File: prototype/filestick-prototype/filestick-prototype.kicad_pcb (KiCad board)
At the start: 4 copper layers, 85 x 75 mm, 60 parts, among them J1 DIN-5, J2 DIN-5, J3 GPIO header 1, J4 UART header, J5 GPIO header 2, J6 SPI header, Q1 2N7002, Q2 2N7002, Q3 2N7002, Q4 2N7002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

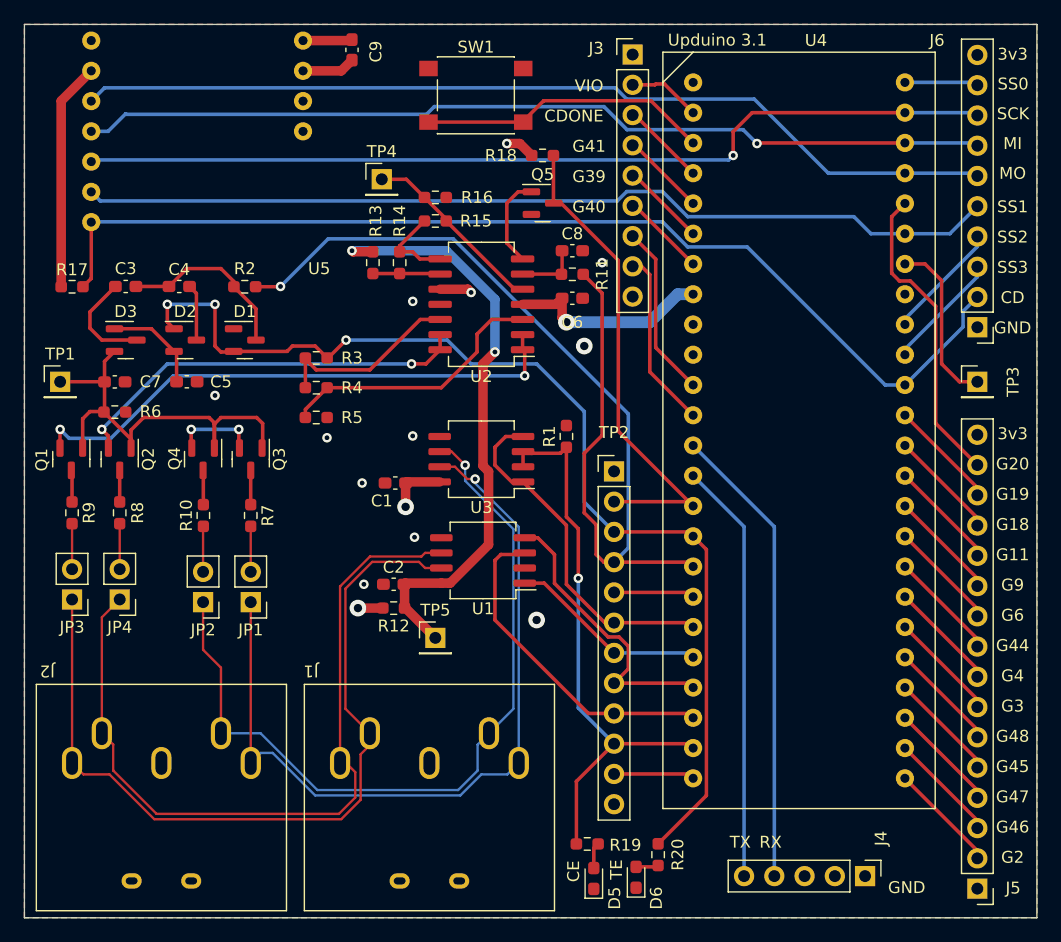
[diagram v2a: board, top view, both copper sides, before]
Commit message: fix prototype PCB errors
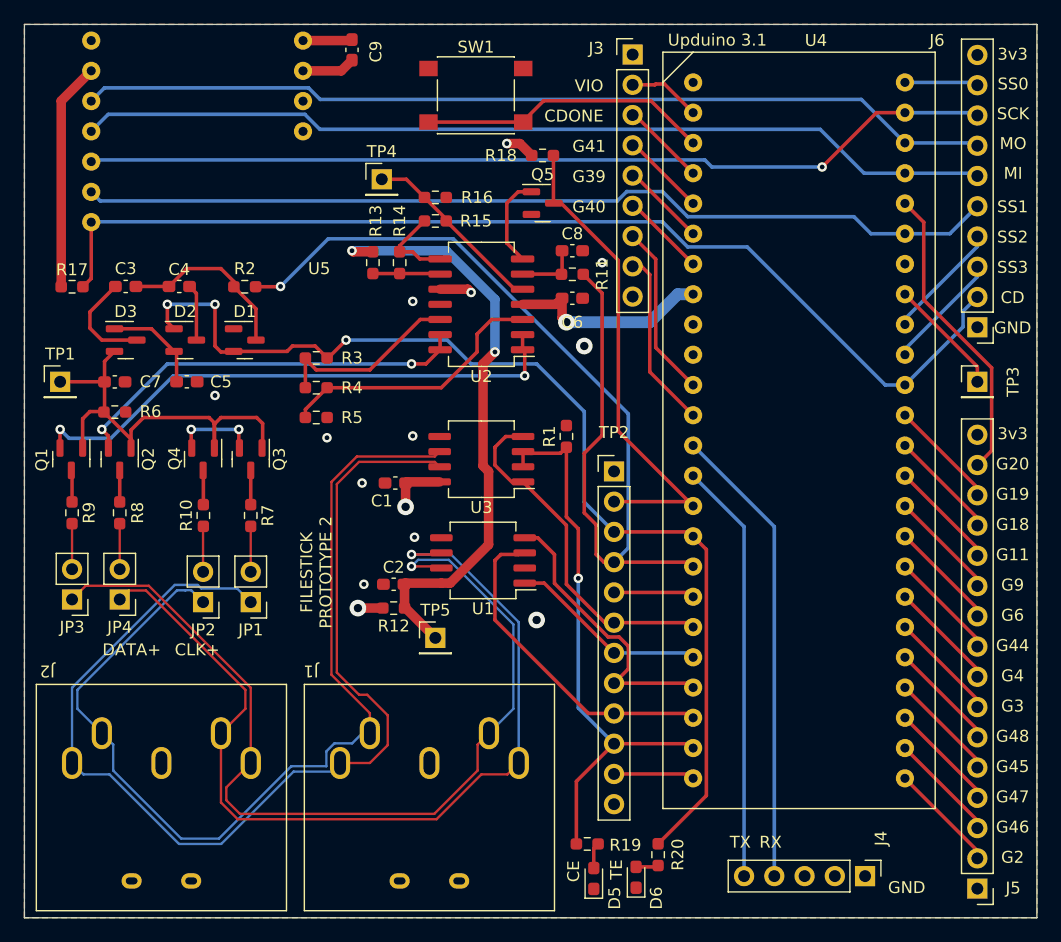
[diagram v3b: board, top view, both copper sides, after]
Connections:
- J6 pad 6: /MOSI -> /MISO
- J6 pad 7: /MISO -> /MOSI
- U4 pad 41: GND -> Net-(TP3-Pad1)
- U4 pad 42: Net-(TP3-Pad1) -> GND
- U4 pad 45: /MOSI -> /MISO
- U4 pad 46: /MISO -> /MOSI
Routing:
- net /CLK-: track 67.6 -> 91.9 mm, vias 1 -> 0
- net /CLK+: track 67.0 -> 83.3 mm, vias 1 -> 0
- net /DATA+: track 66.0 -> 77.9 mm, vias 0 -> 1
- net /DATA-: track 68.7 -> 79.5 mm, vias 0 -> 1
- net Net-(TP3-Pad1): track 14.3 -> 9.87 mm
- net /MOSI: track 77.9 -> 76.9 mm
- net /SCK: track 77.4 -> 76.7 mm
- net /MISO: track 76.7 -> 77.1 mm, vias 1 -> 0
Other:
- board text added: "CLK+"
- board text added: "DATA+"
- board text added: "FILESTICK PROTOTYPE 2"
